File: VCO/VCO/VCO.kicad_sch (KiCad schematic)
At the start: 0 parts

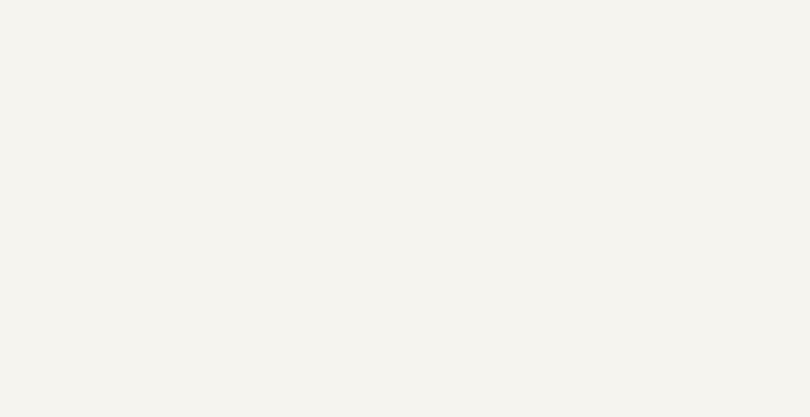
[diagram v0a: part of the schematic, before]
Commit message: mounting holes
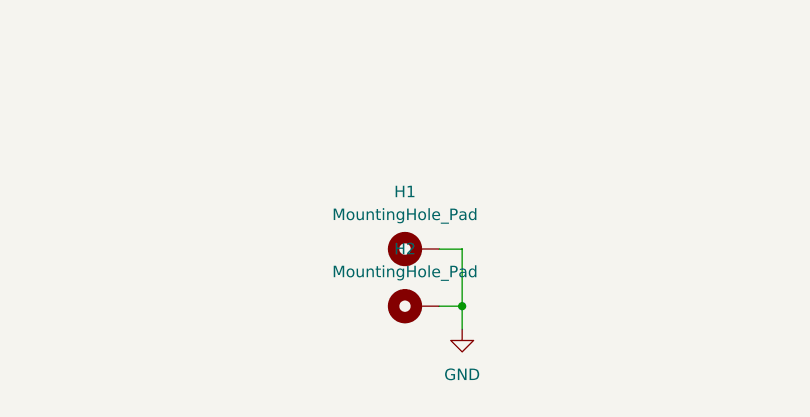
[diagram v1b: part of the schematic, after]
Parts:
- added H1, H2: MountingHole_Pad, MountingHole:MountingHole_3.2mm_M3_DIN965_Pad, symbol Mechanical:MountingHole_Pad
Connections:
- new net GND: H1.1, H2.1
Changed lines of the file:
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@@
 (kicad_sch (version 20230121) (generator eeschema)
   (paper "A4")
+  (junction (at 166.37 109.22) (diameter 0) (color 0 0 0 0)
+  )
+  (wire (pts (xy 163.83 102.87) (xy 166.37 102.87))
+    (stroke (width 0) (type default))
+  )
+  (wire (pts (xy 166.37 109.22) (xy 166.37 111.76))
+    (stroke (width 0) (type default))
+  )
+  (wire (pts (xy 166.37 102.87) (xy 166.37 109.22))
+    (stroke (width 0) (type default))
+  )
+  (wire (pts (xy 163.83 109.22) (xy 166.37 109.22))
+    (stroke (width 0) (type default))
+  )
+  (symbol (lib_id "power:GND") (at 166.37 111.76 0) (unit 1)
+    (in_bom yes) (on_board yes) (dnp no) (fields_autoplaced)
+    (property "Reference" "#PWR059" (at 166.37 118.11 0)
+      (effects (font (size 1.27 1.27)) hide)
+    )
+    (property "Value" "GND" (at 166.37 116.84 0)
+      (effects (font (size 1.27 1.27)))
+    )
+    (property "Footprint" "" (at 166.37 111.76 0)
+      (effects (font (size 1.27 1.27)) hide)
+    )
+    (property "Datasheet" "" (at 166.37 111.76 0)
+      (effects (font (size 1.27 1.27)) hide)
+    )
+    (pin "1")
+    (instances
+      (project "VCO"
+        (path "/07047393-d9d5-4686-952a-e5b55e75d5c3"
+          (reference "#PWR059") (unit 1)
+        )
+      )
+    )
+  )
+  (symbol (lib_id "Mechanical:MountingHole_Pad") (at 161.29 109.22 90) (unit 1)
+    (in_bom yes) (on_board yes) (dnp no) (fields_autoplaced)
+    (property "Reference" "H2" (at 160.02 102.87 90)
+      (effects (font (size 1.27 1.27)))
+    )
+    (property "Value" "MountingHole_Pad" (at 160.02 105.41 90)
+      (effects (font (size 1.27 1.27)))
+    )
+    (property "Footprint" "MountingHole:MountingHole_3.2mm_M3_DIN965_Pad" (at 161.29 109.22 0)
+      (effects (font (size 1.27 1.27)) hide)
+    )
+    (property "Datasheet" "~" (at 161.29 109.22 0)
+      (effects (font (size 1.27 1.27)) hide)
+    )
+    (pin "1")
+    (instances
+      (project "VCO"
+        (path "/07047393-d9d5-4686-952a-e5b55e75d5c3"
+          (reference "H2") (unit 1)
+        )
+      )
+    )
+  )
+  (symbol (lib_id "Mechanical:MountingHole_Pad") (at 161.29 102.87 90) (unit 1)
+    (in_bom yes) (on_board yes) (dnp no) (fields_autoplaced)
+    (property "Reference" "H1" (at 160.02 96.52 90)
+      (effects (font (size 1.27 1.27)))
+    )
+    (property "Value" "MountingHole_Pad" (at 160.02 99.06 90)
+      (effects (font (size 1.27 1.27)))
+    )
+    (property "Footprint" "MountingHole:MountingHole_3.2mm_M3_DIN965_Pad" (at 161.29 102.87 0)
+      (effects (font (size 1.27 1.27)) hide)
+    )
+    (property "Datasheet" "~" (at 161.29 102.87 0)
+      (effects (font (size 1.27 1.27)) hide)
+    )
+    (pin "1")
+    (instances
+      (project "VCO"
+        (path "/07047393-d9d5-4686-952a-e5b55e75d5c3"
+          (reference "H1") (unit 1)
+        )
+      )
+    )
+  )
   (sheet (at 137.16 36.83) (size 86.36 27.94) (fields_autoplaced)
     (stroke (width 0.1524) (type solid))
